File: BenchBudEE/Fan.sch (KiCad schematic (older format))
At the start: 9 parts

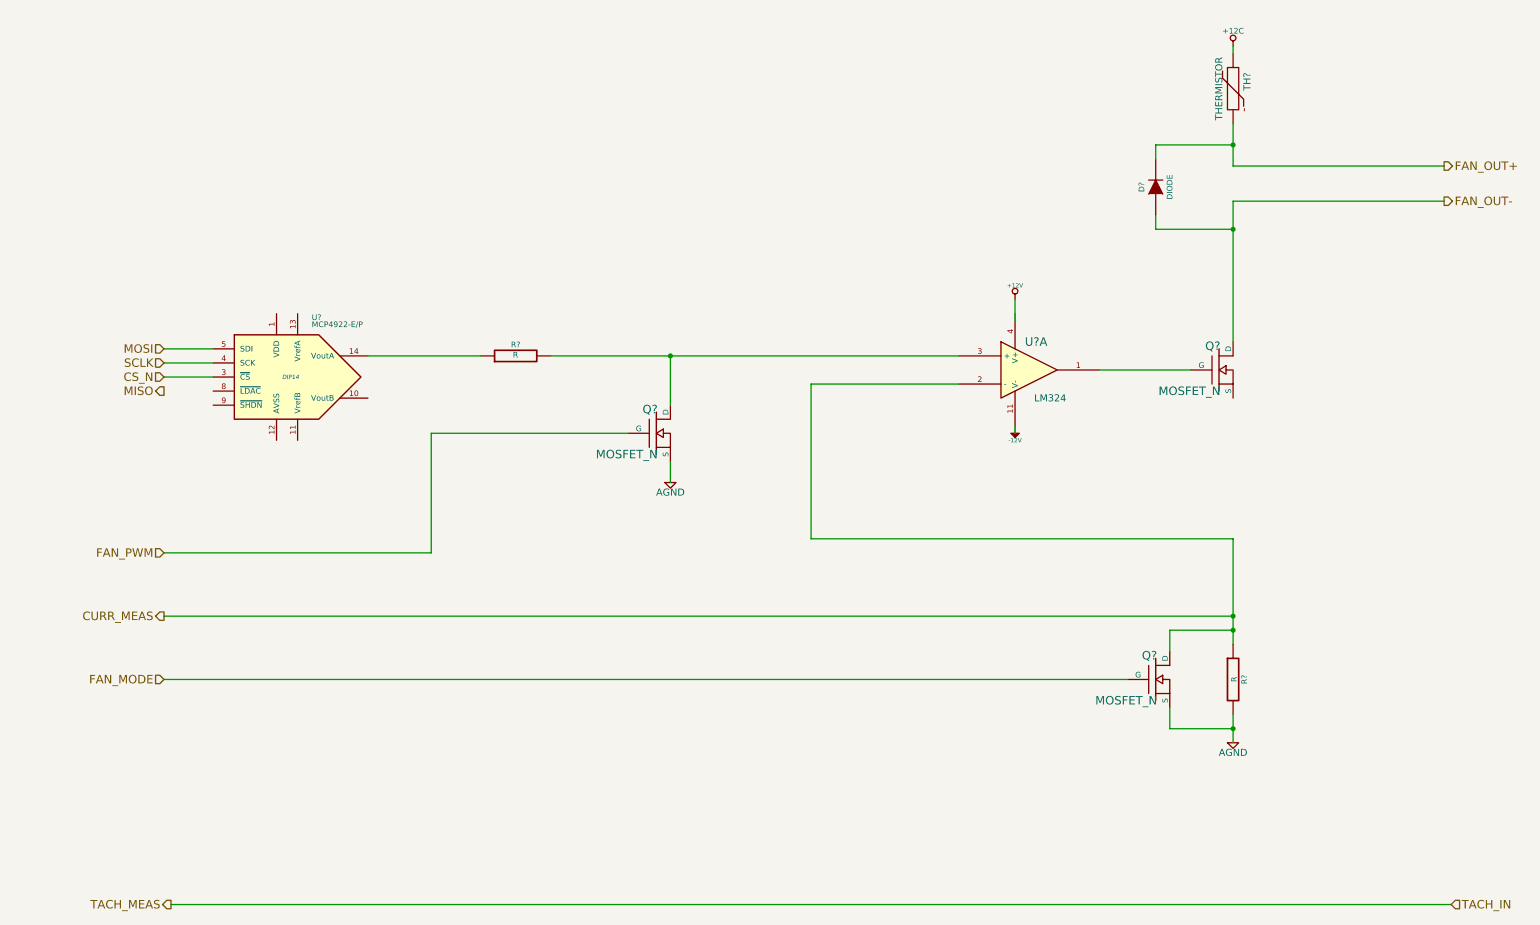
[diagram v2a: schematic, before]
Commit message: Associating and Placing the Relay Module
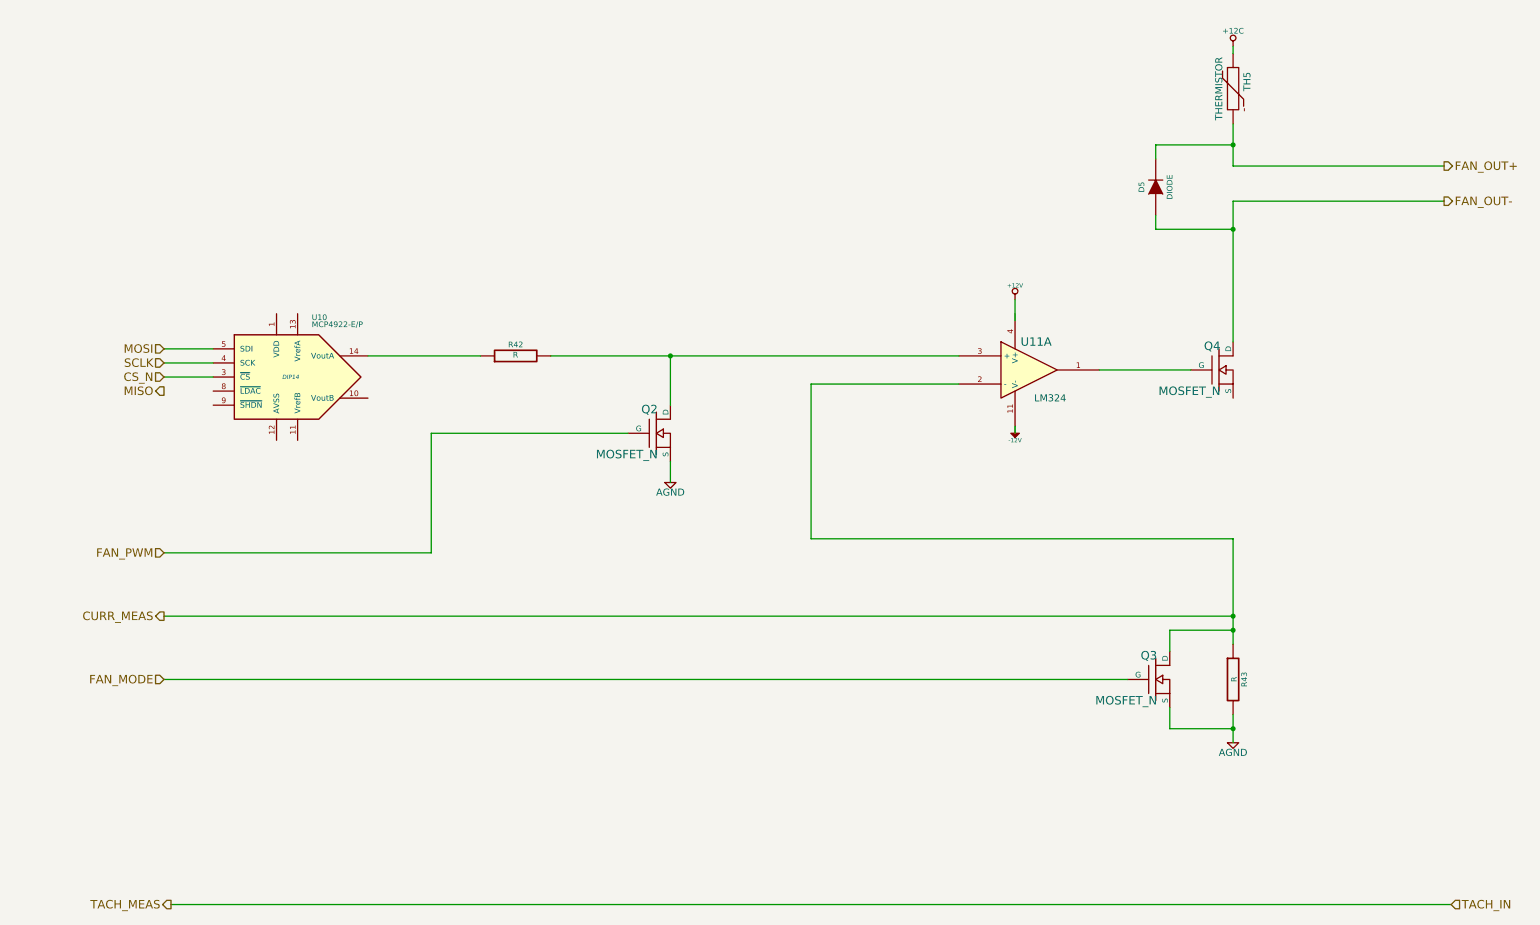
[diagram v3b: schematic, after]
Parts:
- gave numbers to parts that had none: 9
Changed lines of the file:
@@
 FAN_PWM
 $Comp
-L LM324 U?
+L LM324 U11
 U 1 1 52F13D12
 P 7650 3100
-F 0 "U?" H 7700 3300 60  0000 C CNN
+F 0 "U11" H 7700 3300 60  0000 C CNN
 F 1 "LM324" H 7800 2900 50  0000 C CNN
 F 2 "" H 7650 3100 60  0000 C CNN
@@
 $EndComp
 $Comp
-L MOSFET_N Q?
+L MOSFET_N Q4
 U 1 1 52F13D3A
 P 9000 3100
-F 0 "Q?" H 9010 3270 60  0000 R CNN
+F 0 "Q4" H 9010 3270 60  0000 R CNN
 F 1 "MOSFET_N" H 9010 2950 60  0000 R CNN
 F 2 "~" H 9000 3100 60  0000 C CNN
@@
 	9100 4300 9100 5050
 $Comp
-L R R?
+L R R43
 U 1 1 52F13D66
 P 9100 5300
-F 0 "R?" V 9180 5300 40  0000 C CNN
+F 0 "R43" V 9180 5300 40  0000 C CNN
 F 1 "R" V 9107 5301 40  0000 C CNN
 F 2 "~" V 9030 5300 30  0000 C CNN
@@
 $EndComp
 $Comp
-L AGND #PWR048
+L AGND #PWR55
 U 1 1 52F13D75
 P 9100 5750
-F 0 "#PWR048" H 9100 5750 40  0001 C CNN
+F 0 "#PWR55" H 9100 5750 40  0001 C CNN
 F 1 "AGND" H 9100 5680 50  0000 C CNN
 F 2 "" H 9100 5750 60  0000 C CNN
@@
 	6100 3200 7150 3200
 $Comp
-L +12V #PWR049
+L +12V #PWR52
 U 1 1 52F13D90
 P 7550 2600
-F 0 "#PWR049" H 7550 2550 20  0001 C CNN
+F 0 "#PWR52" H 7550 2550 20  0001 C CNN
 F 1 "+12V" H 7550 2700 30  0000 C CNN
 F 2 "" H 7550 2600 60  0000 C CNN
@@
 $EndComp
 $Comp
-L -12V #PWR050
+L -12V #PWR53
 U 1 1 52F13D98
 P 7550 3500
-F 0 "#PWR050" H 7550 3630 20  0001 C CNN
+F 0 "#PWR53" H 7550 3630 20  0001 C CNN
 F 1 "-12V" H 7550 3600 30  0000 C CNN
 F 2 "" H 7550 3500 60  0000 C CNN
@@
 	5100 3750 5100 3900
 $Comp
-L AGND #PWR051
+L AGND #PWR51
 U 1 1 52F13E8F
 P 5100 3900
-F 0 "#PWR051" H 5100 3900 40  0001 C CNN
+F 0 "#PWR51" H 5100 3900 40  0001 C CNN
 F 1 "AGND" H 5100 3830 50  0000 C CNN
 F 2 "" H 5100 3900 60  0000 C CNN
@@
 $EndComp
 $Comp
-L MCP4922-E/P U?
+L MCP4922-E/P U10
 U 1 1 52F13EA6
 P 2400 3150
-F 0 "U?" H 2550 3550 40  0000 L BNN
+F 0 "U10" H 2550 3550 40  0000 L BNN
 F 1 "MCP4922-E/P" H 2550 3500 40  0000 L BNN
 F 2 "DIP14" H 2400 3150 30  0000 C CIN
@@
 Connection ~ 9100 4850
 $Comp
-L R R?
+L R R42
 U 1 1 52F13FEC
 P 4000 3000
-F 0 "R?" V 4080 3000 40  0000 C CNN
+F 0 "R42" V 4080 3000 40  0000 C CNN
 F 1 "R" V 4007 3001 40  0000 C CNN
 F 2 "~" V 3930 3000 30  0000 C CNN
@@
 	1500 3150 1850 3150
 $Comp
-L MOSFET_N Q?
+L MOSFET_N Q3
 U 1 1 52FA6D72
 P 8550 5300
-F 0 "Q?" H 8560 5470 60  0000 R CNN
+F 0 "Q3" H 8560 5470 60  0000 R CNN
 F 1 "MOSFET_N" H 8560 5150 60  0000 R CNN
 F 2 "~" H 8550 5300 60  0000 C CNN
@@
 $EndComp
 $Comp
-L THERMISTOR TH?
+L THERMISTOR TH5
 U 1 1 52FA6DA7
 P 9100 1100
-F 0 "TH?" V 9200 1150 50  0000 C CNN
+F 0 "TH5" V 9200 1150 50  0000 C CNN
 F 1 "THERMISTOR" V 9000 1100 50  0000 C CNN
 F 2 "~" H 9100 1100 60  0000 C CNN
@@
 	10600 1900 9100 1900
 $Comp
-L DIODE D?
+L DIODE D5
 U 1 1 52FA6E1D
 P 8550 1800
-F 0 "D?" H 8550 1900 40  0000 C CNN
+F 0 "D5" H 8550 1900 40  0000 C CNN
 F 1 "DIODE" H 8550 1700 40  0000 C CNN
 F 2 "~" H 8550 1800 60  0000 C CNN
@@
 	1500 4400 3400 4400
 $Comp
-L MOSFET_N Q?
+L MOSFET_N Q2
 U 1 1 52FA7001
 P 5000 3550
-F 0 "Q?" H 5010 3720 60  0000 R CNN
+F 0 "Q2" H 5010 3720 60  0000 R CNN
 F 1 "MOSFET_N" H 5010 3400 60  0000 R CNN
 F 2 "~" H 5000 3550 60  0000 C CNN
@@
 FAN_MODE
 $Comp
-L +12C #PWR052
+L +12C #PWR54
 U 1 1 52FA7706
 P 9100 800
-F 0 "#PWR052" H 9100 770 30  0001 C CNN
+F 0 "#PWR54" H 9100 770 30  0001 C CNN
 F 1 "+12C" H 9100 910 40  0000 C CNN
 F 2 "" H 9100 800 60  0000 C CNN

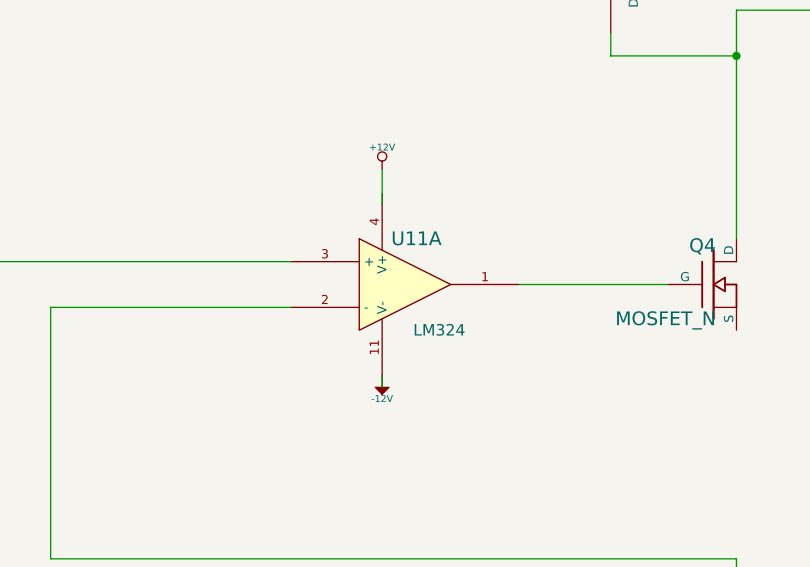
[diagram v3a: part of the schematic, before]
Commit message: Associating and Placingthe Thermocouple Module
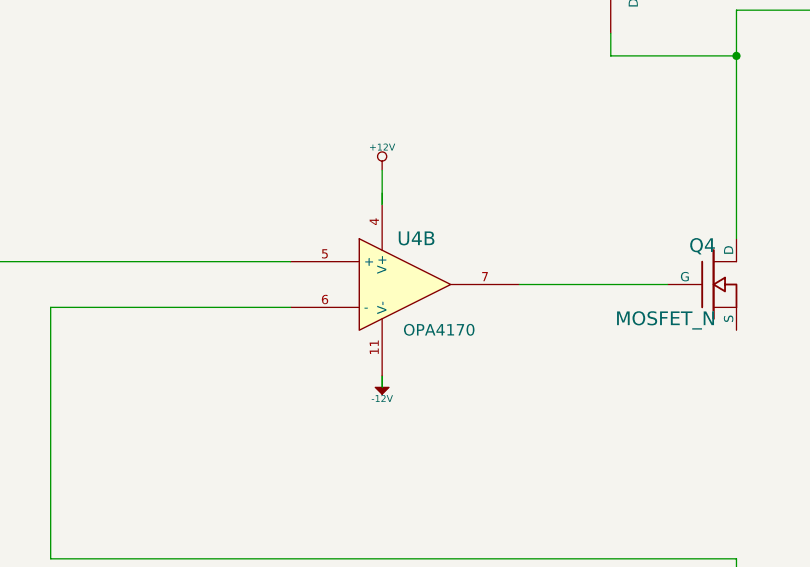
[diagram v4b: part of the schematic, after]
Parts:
- U4: renamed from U11; value LM324 -> OPA4170
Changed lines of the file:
@@
 $Descr A4 11693 8268
 encoding utf-8
-Sheet 6 9
+Sheet 9 9
 Title ""
-Date "17 feb 2014"
+Date "19 feb 2014"
 Rev ""
 Comp ""
@@
 FAN_PWM
 $Comp
-L LM324 U11
-U 1 1 52F13D12
+L LM324 U4
+U 2 1 52F13D12
 P 7650 3100
-F 0 "U11" H 7700 3300 60  0000 C CNN
-F 1 "LM324" H 7800 2900 50  0000 C CNN
+F 0 "U4" H 7700 3300 60  0000 C CNN
+F 1 "OPA4170" H 7800 2900 50  0000 C CNN
 F 2 "" H 7650 3100 60  0000 C CNN
 F 3 "" H 7650 3100 60  0000 C CNN
-	1    7650 3100
+	2    7650 3100
 	1    0    0    -1
 $EndComp
@@
 $EndComp
 $Comp
-L AGND #PWR55
+L AGND #PWR056
 U 1 1 52F13D75
 P 9100 5750
-F 0 "#PWR55" H 9100 5750 40  0001 C CNN
+F 0 "#PWR056" H 9100 5750 40  0001 C CNN
 F 1 "AGND" H 9100 5680 50  0000 C CNN
 F 2 "" H 9100 5750 60  0000 C CNN
@@
 	6100 3200 7150 3200
 $Comp
-L +12V #PWR52
+L +12V #PWR057
 U 1 1 52F13D90
 P 7550 2600
-F 0 "#PWR52" H 7550 2550 20  0001 C CNN
+F 0 "#PWR057" H 7550 2550 20  0001 C CNN
 F 1 "+12V" H 7550 2700 30  0000 C CNN
 F 2 "" H 7550 2600 60  0000 C CNN
@@
 $EndComp
 $Comp
-L -12V #PWR53
+L -12V #PWR058
 U 1 1 52F13D98
 P 7550 3500
-F 0 "#PWR53" H 7550 3630 20  0001 C CNN
+F 0 "#PWR058" H 7550 3630 20  0001 C CNN
 F 1 "-12V" H 7550 3600 30  0000 C CNN
 F 2 "" H 7550 3500 60  0000 C CNN
@@
 	5100 3750 5100 3900
 $Comp
-L AGND #PWR51
+L AGND #PWR059
 U 1 1 52F13E8F
 P 5100 3900
-F 0 "#PWR51" H 5100 3900 40  0001 C CNN
+F 0 "#PWR059" H 5100 3900 40  0001 C CNN
 F 1 "AGND" H 5100 3830 50  0000 C CNN
 F 2 "" H 5100 3900 60  0000 C CNN
@@
 FAN_MODE
 $Comp
-L +12C #PWR54
+L +12C #PWR060
 U 1 1 52FA7706
 P 9100 800
-F 0 "#PWR54" H 9100 770 30  0001 C CNN
+F 0 "#PWR060" H 9100 770 30  0001 C CNN
 F 1 "+12C" H 9100 910 40  0000 C CNN
 F 2 "" H 9100 800 60  0000 C CNN
